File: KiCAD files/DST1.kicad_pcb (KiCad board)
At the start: 2 copper layers, 50 x 100 mm, 58 parts, among them J1 SN49B14B, J2 SN49B14B, J3 Barrel_Jack_MountingPin, J4 Conn_01x03_Pin, J5 Conn_01x03_Pin, J6 Conn_01x03_Pin, Q1 2N3904, Q2 2N3904, Q3 2N3904, U1 TL072

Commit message: Update
I updated the schematic and finished the PCB, might need to upload new photos tho.
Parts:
- removed the J4 at (147.9, 123.7)
- removed the J5 at (152.6, 123.7)
- removed J6: Conn_01x03_Pin, Connector_PinHeader_2.54mm:PinHeader_1x03_P2.54mm_Vertical
- added C1: 470nF, Capacitor_THT:C_Rect_L4.6mm_W3.0mm_P2.50mm_MKS02_FKP02, F.Cu at (150.2, 94.7)
- added FTSW1: ~, Library:3PDT Footswitch, F.Cu at (152.5, 129.5)
- moved D2 6.21 mm to (151.5, 87.5)
- renumbered C9 to C10, C10 to C11, C11 to C12, C12 to C13, C13 to C14, C14 to C15, C1 to C2, C2 to C3, C3 to C4, C4 to C5, C5 to C6, C6 to C8, C8 to C9, D4 to D1, D5 to D2, D1 to D3, D2 to D4, D3 to D5, J1 to J4, J2 to J5, R7 to R10, R8 to R11, R9 to R12, R10 to R13, R11 to R14, R12 to R15, R13 to R16, R14 to R17, R15 to R18, R16 to R19, R17 to R20, R18 to R21, R19 to R22, R20 to R23, R21 to R24, R22 to R25, R23 to R26, R24 to R5, R25 to R6, R26 to R7, R5 to R8, R6 to R9
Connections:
- net Net-(J5-Pin_1) renamed DST_IN
- net Net-(J6-Pin_1) renamed DST_OUT
- R2 pad 2: Net-(Q1-B) -> Net-(C1-Pad1)
- R8 pad 1: GND -> +4.5V
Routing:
- net Vbatt: track 26.9 -> 119.7 mm
- net +BATT: track 89.6 -> 0.00 mm
- net +9V: track 73.7 -> 97.1 mm
- net out: track 58.1 -> 70.8 mm
- net DST_OUT: track 25.8 -> 37.9 mm
- net DST_IN: track 48.2 -> 58.2 mm
- net in: track 48.5 -> 58.0 mm
- net Net-(Q3-B): track 54.7 -> 50.8 mm
- removed copper zone on B.Cu, net GND
- removed copper zone on F.Cu, net GND
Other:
- board text added: "DST-1"
- board text removed: "BOSS DS-1"
- board text removed: "DST - 1 Tudor S. {dblquote}Flăcărică{dblquote}"
- board text removed: "Footswitch 3PDT"

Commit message: Update
I updated the schematic PDF and the photo renders of the board
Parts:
- added ?: , , F.Cu at (172.5, 134.5)
- added ?: , , F.Cu at (137.5, 44.6)
- added ?: , , F.Cu at (167.5, 44.5)
- added ?: , , F.Cu at (132.5, 134.5)
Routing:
- net +4.5V: track 160.3 -> 175.4 mm
- net Net-(C1-Pad1): track 0.00 -> 9.20 mm
- net Vbatt: track 119.7 -> 112.9 mm
- net in: track 58.0 -> 52.9 mm
- net Net-(Q1-B): track 8.41 -> 12.8 mm
- net DST_IN: track 58.2 -> 61.8 mm
- added copper zone on B.Cu, net GND
- added copper zone on F.Cu, net GND

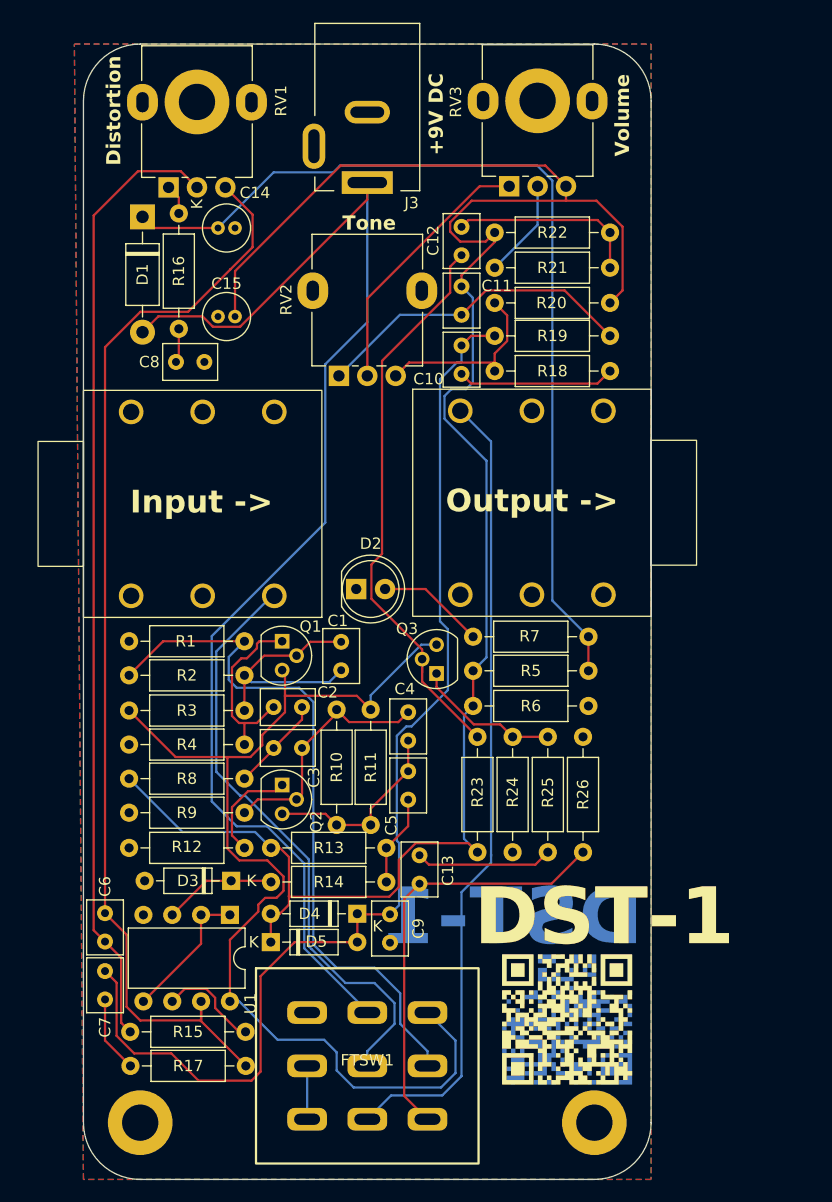
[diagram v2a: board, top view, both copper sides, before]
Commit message: Updated schematic and PCB
I chose the wrong values for some resistors and capacitors, and so I had to update the schematic. I also wired the footswitch in a wrong manner and so I had to update the PCB.
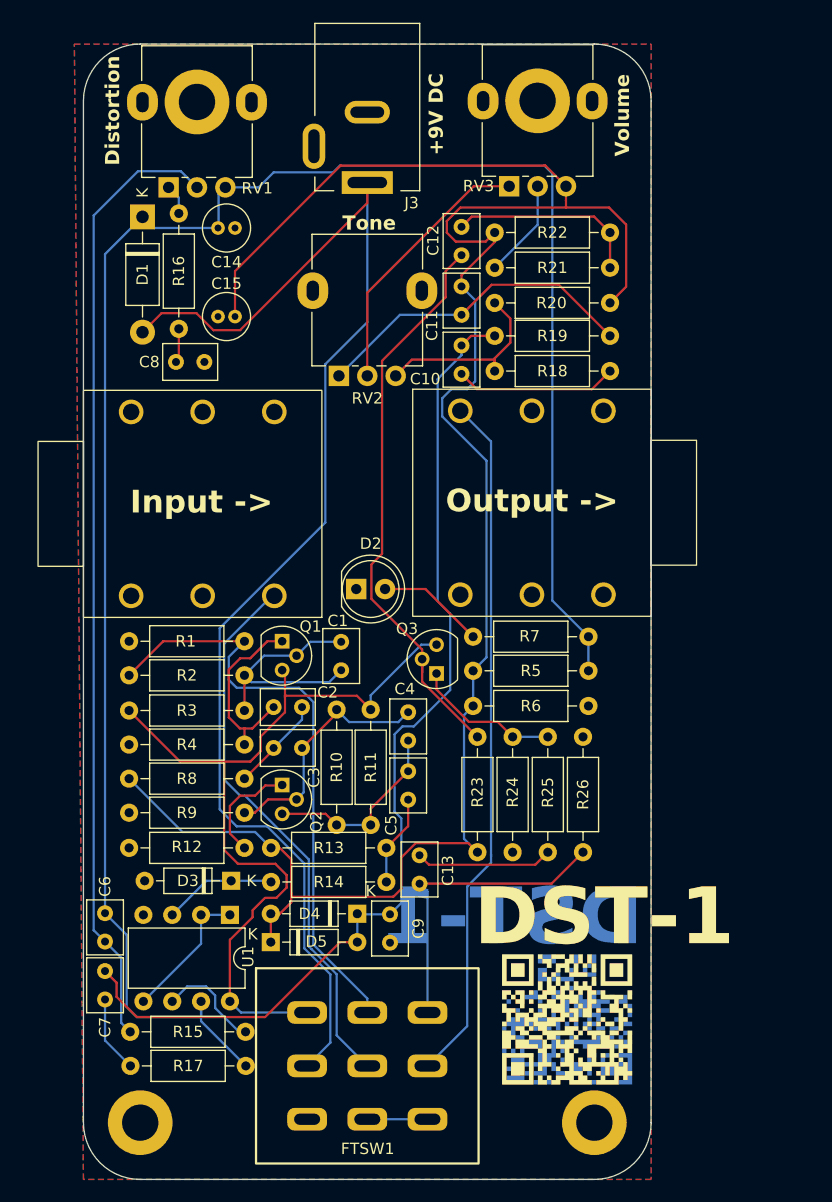
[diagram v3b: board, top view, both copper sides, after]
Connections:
- ? pad 1: (no net) -> GND (x4)
- C14 pad 1: Net-(D1-K) -> Net-(C6-Pad2)
- D1 pad 1: Net-(D1-K) -> Net-(C6-Pad2)
- J3 pad 3: (no net) -> GND
- J4 pad SB: (no net) -> GND
- J5 pad SB: (no net) -> GND
- R5 pad 2: Net-(D1-K) -> Net-(C6-Pad2)
- R7 pad 2: Net-(D1-K) -> Net-(C6-Pad2)
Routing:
- net Net-(D1-K): track 83.8 -> 0.00 mm
- net Net-(C6-Pad2): track 97.9 -> 173.3 mm
- net +9V: track 97.1 -> 74.5 mm
- net Net-(D4-K): track 101.6 -> 90.7 mm
- net DST_OUT: track 37.9 -> 27.4 mm
- net out: track 70.8 -> 61.3 mm
- net DST_IN: track 61.8 -> 52.9 mm
- net Vbatt: track 112.9 -> 117.2 mm
- net in: track 52.9 -> 48.8 mm
- net +4.5V: track 175.4 -> 177.5 mm
- net bypass: track 4.70 -> 5.30 mm
- net Net-(R18-Pad2): track 16.9 -> 17.5 mm

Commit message: Updated the PCB
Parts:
- removed the R1 at (141.7, 92.1)
- C1: value 470nF -> 47nF
- C10: value 100pF -> 22nF
- C11, C9: value 100pF -> 10nF
- R15: renamed from R20; value 2.2kΩ -> 6.8kΩ
- RV3: value 20kΩ -> 100kΩ
- moved C8 8.82 mm to (138.2, 123.0), turned to 0 degrees
- moved C6 5.48 mm to (132.6, 123.0), turned to 0 degrees
- moved U1 3.80 mm to (140.5, 112.4)
- moved D1 3.20 mm to (140.4, 110.0)
- moved R8 3.10 mm to (131.6, 107.2)
- moved R1 3.00 mm to (131.6, 92.1)
- moved R2 3.00 mm to (131.6, 95.2)
- moved R3 3.00 mm to (131.6, 98.2)
- moved R4 3.00 mm to (131.6, 101.2)
- moved R5 3.00 mm to (131.6, 104.2)
- renumbered C8 to C7, C7 to C8, D3 to D1, D4 to D2, D5 to D3, D1 to D4, D2 to D5, R2 to R1, R14 to R10, R15 to R11, R16 to R12, R17 to R13, R18 to R14, R19 to R16, R21 to R17, R22 to R18, R23 to R19, R3 to R2, R24 to R20, R25 to R21, R26 to R22, R5 to R23, R6 to R24, R7 to R25, R4 to R3, R8 to R4, R9 to R5, R10 to R6, R11 to R7, R12 to R8, R13 to R9
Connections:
- C14 pad 1: Net-(C6-Pad2) -> Net-(D4-K)
- D4 pad 1: Net-(C6-Pad2) -> Net-(D4-K)
- R23 pad 2: Net-(C6-Pad2) -> Net-(D4-K)
- R25 pad 2: Net-(C6-Pad2) -> Net-(D4-K)
- RV3 pad 1: Net-(RV2-Pad2) -> +4.5V
- RV3 pad 3: +4.5V -> Net-(RV2-Pad2)
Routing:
- net GND: track 0.00 -> 151.9 mm
- net Net-(C6-Pad2): track 173.3 -> 83.1 mm
- net Net-(D4-K): track 0.00 -> 71.6 mm
- net +4.5V: track 177.5 -> 159.8 mm
- net +9V: track 74.5 -> 89.4 mm, vias 0 -> 1
- net Net-(D2-K): track 90.7 -> 80.3 mm
- net Net-(R17-Pad1): track 8.74 -> 19.0 mm
- net Net-(RV2-Pad2): track 23.7 -> 32.3 mm
- net Net-(Q1-E): track 16.6 -> 9.26 mm
- net Net-(C6-Pad1): track 84.5 -> 78.7 mm
- net Net-(Q2-E): track 9.59 -> 4.21 mm
- net Net-(C1-Pad1): track 9.20 -> 13.9 mm
- net DST_IN: track 52.9 -> 48.3 mm
- net Net-(Q3-B): track 50.8 -> 46.9 mm
- net Net-(U1B--): track 9.31 -> 12.8 mm
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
